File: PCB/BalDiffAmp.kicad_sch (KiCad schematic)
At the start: 19 parts, among them U11 OPA1622

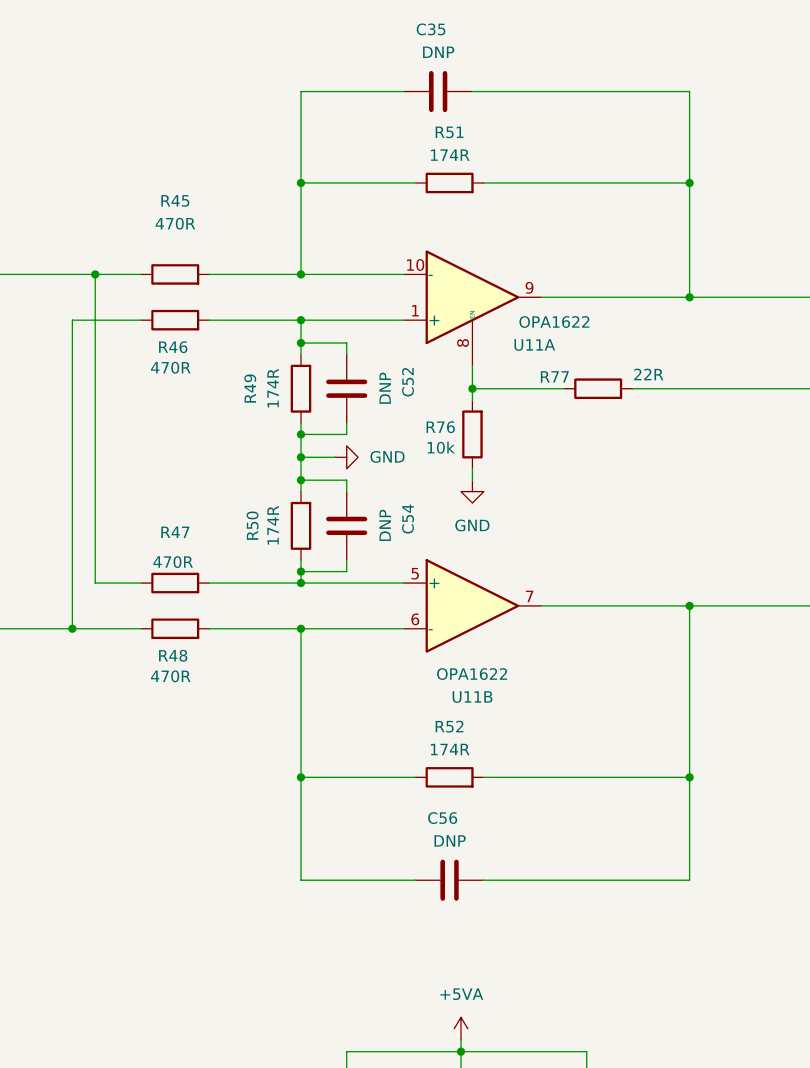
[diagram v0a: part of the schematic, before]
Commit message: Optimized designator positions and DNP for capacitors in OPA1622
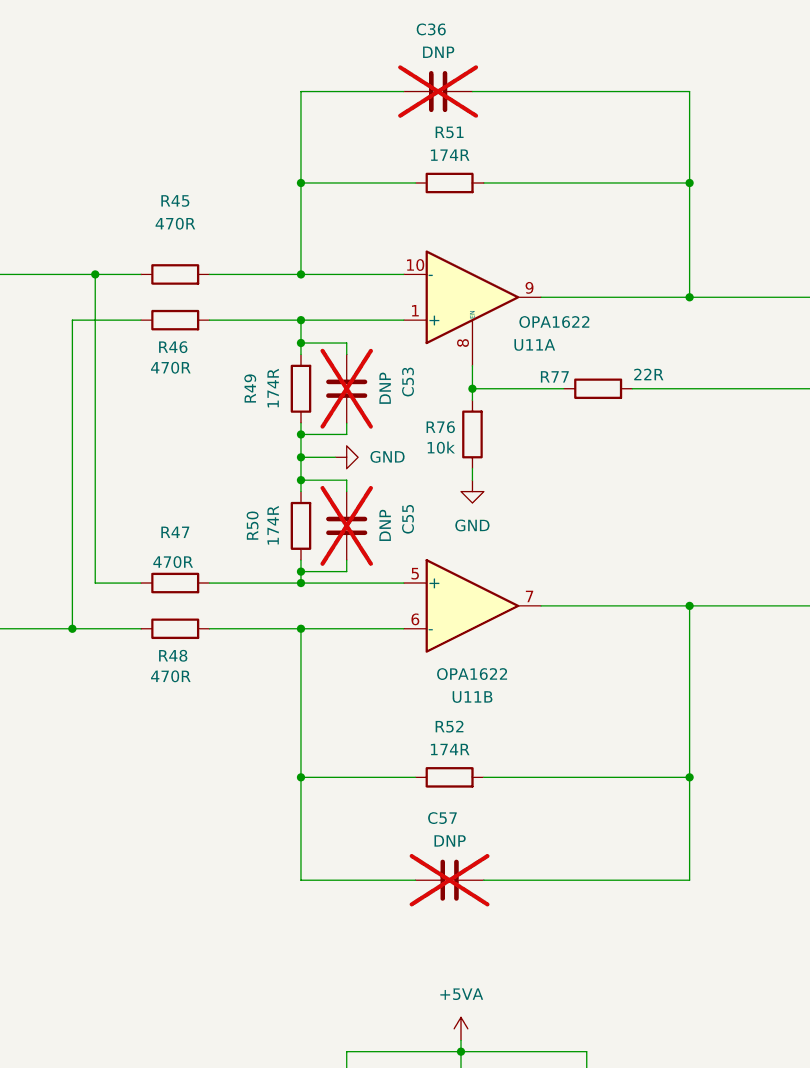
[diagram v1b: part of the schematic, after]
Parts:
- C36: renamed from C35; now not fitted
- C53: renamed from C52; now not fitted
- C55: renamed from C54; now not fitted
- C57: renamed from C56; now not fitted
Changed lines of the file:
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@@
 		(in_bom yes)
 		(on_board yes)
-		(dnp no)
-		(property "Reference" "C35"
+		(dnp yes)
+		(property "Reference" "C36"
 			(at 137.668 28.702 90)
 			(effects
@@
 		(in_bom yes)
 		(on_board yes)
-		(dnp no)
-		(property "Reference" "C54"
+		(dnp yes)
+		(property "Reference" "C55"
 			(at 135.128 83.058 90)
 			(effects
@@
 		(in_bom yes)
 		(on_board yes)
-		(dnp no)
-		(property "Reference" "C52"
+		(dnp yes)
+		(property "Reference" "C53"
 			(at 135.128 67.818 90)
 			(effects
@@
 		(in_bom yes)
 		(on_board yes)
-		(dnp no)
-		(property "Reference" "C56"
+		(dnp yes)
+		(property "Reference" "C57"
 			(at 138.938 116.332 90)
 			(effects

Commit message: Redone placement and layout of OPA1622. Still finishing touches
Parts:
- removed C66, C67: 1uF, Capacitor_SMD:C_0603_1608Metric_Pad1.08x0.95mm_HandSolder, symbol Device:C
- removed R76: 10k, Resistor_SMD:R_0402_1005Metric_Pad0.72x0.64mm_HandSolder, symbol Device:R
- removed R77: 22R, Resistor_SMD:R_0402_1005Metric_Pad0.72x0.64mm_HandSolder, symbol Device:R
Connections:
- net BALDIFFAMP_ENABLE: now also U11.8 (EN)

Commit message: Changed the BOM field for JLCPCB to the original name instead of LCSC
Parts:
- C64, C65: JLCPCB Part # (none) -> C1525; LCSC Part # C1525 -> (none)
- R45, R46, R47, R48: JLCPCB Part # (none) -> C445590; LCSC Part # C445590 -> (none)
- R49, R50, R51, R52: JLCPCB Part # (none) -> C852566; LCSC Part # C852566 -> (none)
- U11: JLCPCB Part # (none) -> C2876559; LCSC Part # C2876559 -> (none)
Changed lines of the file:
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@@
 			)
 		)
-		(property "LCSC Part #" "C852566"
+		(property "JLCPCB Part #" "C852566"
 			(at 139.7 45.72 0)
 			(effects
@@
 			)
 		)
-		(property "LCSC Part #" "C1525"
+		(property "JLCPCB Part #" "C1525"
 			(at 128.27 148.59 0)
 			(effects
@@
 		)
 		(property "Voltage" "50V"
-			(at 138.43 35.56 0)
-			(effects
-				(font
-					(size 1.27 1.27)
-				)
-				(hide yes)
-			)
-		)
-		(property "LCSC Part #" ""
 			(at 138.43 35.56 0)
 			(effects
@@
 			)
 		)
-		(property "LCSC Part #" "C2876559"
+		(property "JLCPCB Part #" "C2876559"
 			(at 142.24 92.71 0)
 			(effects
@@
 			)
 		)
-		(property "LCSC Part #" "C445590"
+		(property "JLCPCB Part #" "C445590"
 			(at 109.22 60.96 0)
 			(effects
@@
 			)
 		)
-		(property "LCSC Part #" ""
-			(at 128.27 83.82 0)
-			(effects
-				(font
-					(size 1.27 1.27)
-				)
-				(hide yes)
-			)
-		)
 		(pin "2"
 		)
@@
 			)
 		)
-		(property "LCSC Part #" "C445590"
+		(property "JLCPCB Part #" "C445590"
 			(at 109.22 95.25 0)
 			(effects
@@
 			)
 		)
-		(property "LCSC Part #" "C2876559"
+		(property "JLCPCB Part #" "C2876559"
 			(at 157.48 152.4 0)
 			(effects
@@
 			)
 		)
-		(property "LCSC Part #" "C1525"
+		(property "JLCPCB Part #" "C1525"
 			(at 128.27 161.29 0)
 			(effects
@@
 			)
 		)
-		(property "LCSC Part #" "C852566"
+		(property "JLCPCB Part #" "C852566"
 			(at 123.19 83.82 0)
 			(effects
@@
 			)
 		)
-		(property "LCSC Part #" "C2876559"
+		(property "JLCPCB Part #" "C2876559"
 			(at 142.24 58.42 0)
 			(effects
@@
 		)
 		(property "Voltage" "50V"
-			(at 128.27 68.58 0)
-			(effects
-				(font
-					(size 1.27 1.27)
-				)
-				(hide yes)
-			)
-		)
-		(property "LCSC Part #" ""
 			(at 128.27 68.58 0)
 			(effects
@@
 			)
 		)
-		(property "LCSC Part #" ""
-			(at 139.7 123.19 0)
-			(effects
-				(font
-					(size 1.27 1.27)
-				)
-				(hide yes)
-			)
-		)
 		(pin "2"
 		)
@@
 			)
 		)
-		(property "LCSC Part #" "C445590"
+		(property "JLCPCB Part #" "C445590"
 			(at 109.22 90.17 0)
 			(effects
@@
 			)
 		)
-		(property "LCSC Part #" "C445590"
+		(property "JLCPCB Part #" "C445590"
 			(at 109.22 55.88 0)
 			(effects
@@
 			)
 		)
-		(property "LCSC Part #" "C852566"
+		(property "JLCPCB Part #" "C852566"
 			(at 139.7 111.76 0)
 			(effects
@@
 			)
 		)
-		(property "LCSC Part #" "C852566"
+		(property "JLCPCB Part #" "C852566"
 			(at 123.19 68.58 0)
 			(effects

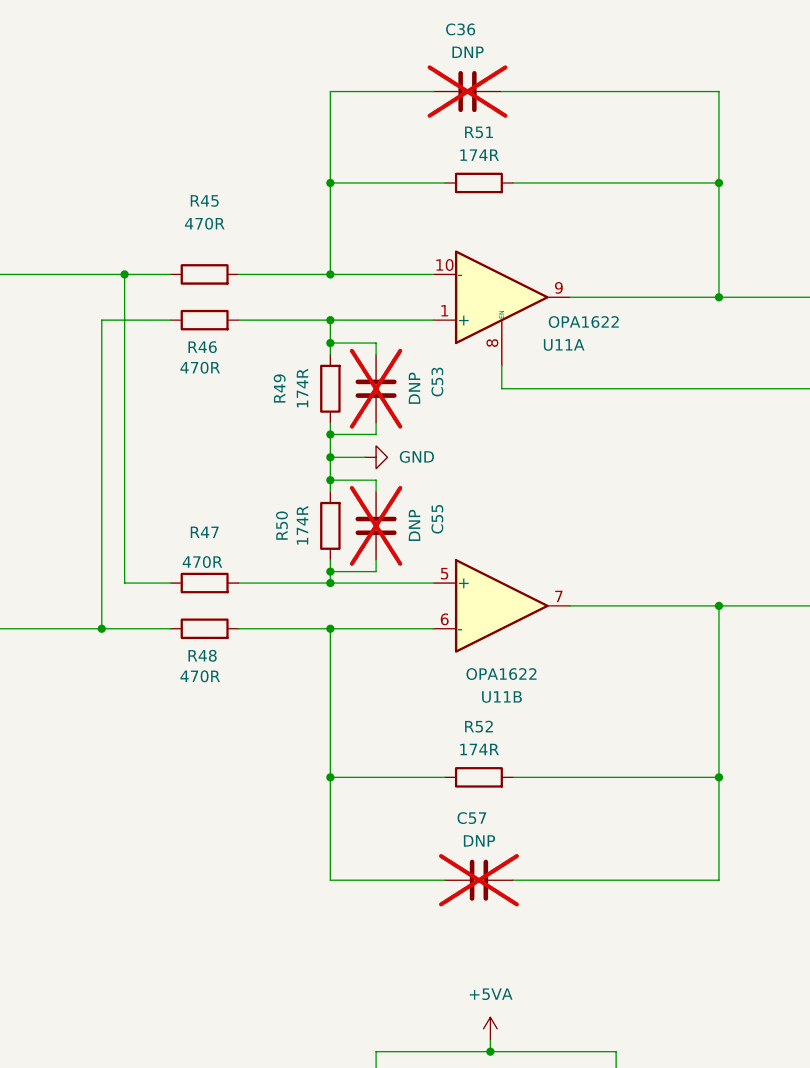
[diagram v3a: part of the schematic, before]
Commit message: Changed single ended connector for gold plated part and changed resistor and capacitor values of opa1622 amp for improved power on high impedance headphones
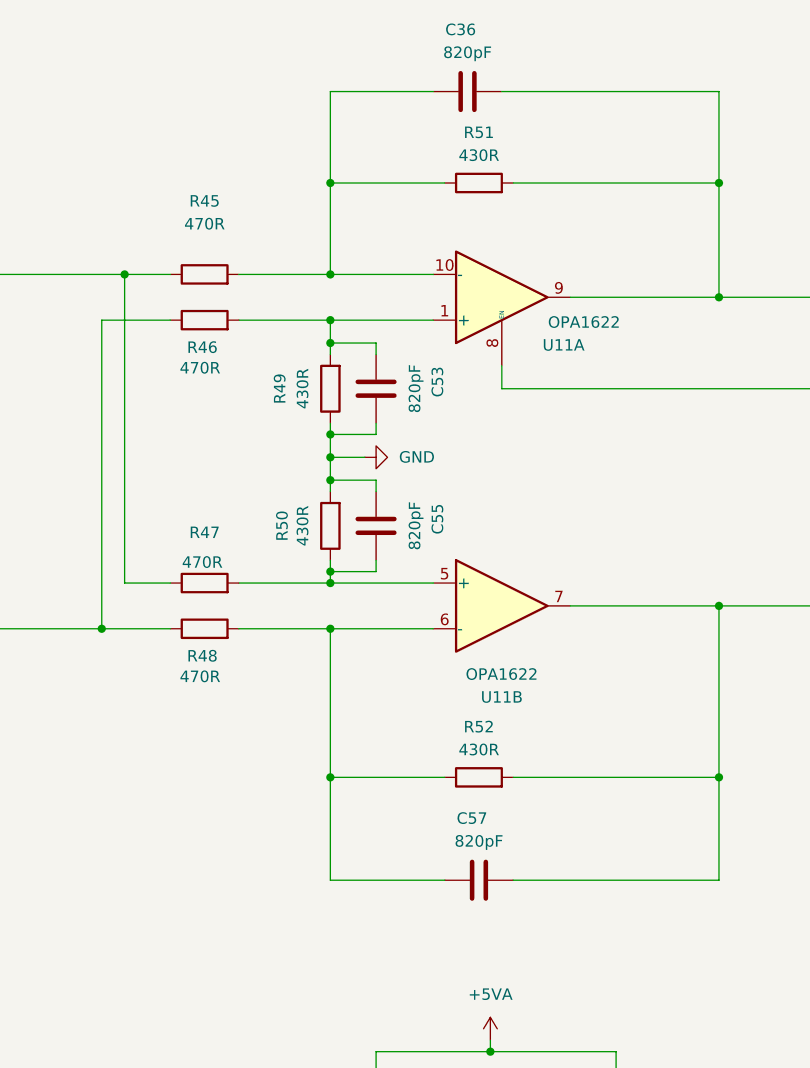
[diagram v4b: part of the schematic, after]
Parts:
- C36, C53, C55, C57: value DNP -> 820pF; JLCPCB Part # (none) -> C99081; now fitted
- R49, R50, R51, R52: value 174R -> 430R; JLCPCB Part # C852566 -> C186317
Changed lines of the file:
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@@
 			)
 		)
-		(property "Value" "174R"
+		(property "Value" "430R"
 			(at 139.7 42.672 90)
 			(effects
@@
 			)
 		)
-		(property "JLCPCB Part #" "C852566"
+		(property "JLCPCB Part #" "C186317"
 			(at 139.7 45.72 0)
 			(effects
@@
 		(in_bom yes)
 		(on_board yes)
-		(dnp yes)
+		(dnp no)
 		(property "Reference" "C36"
 			(at 137.668 28.702 90)
@@
 			)
 		)
-		(property "Value" "DNP"
+		(property "Value" "820pF"
 			(at 138.43 31.242 90)
 			(effects
@@
 		)
 		(property "Voltage" "50V"
+			(at 138.43 35.56 0)
+			(effects
+				(font
+					(size 1.27 1.27)
+				)
+				(hide yes)
+			)
+		)
+		(property "JLCPCB Part #" "C99081"
 			(at 138.43 35.56 0)
 			(effects
@@
 		(in_bom yes)
 		(on_board yes)
-		(dnp yes)
+		(dnp no)
 		(property "Reference" "C55"
 			(at 135.128 83.058 90)
@@
 			)
 		)
-		(property "Value" "DNP"
+		(property "Value" "820pF"
 			(at 132.588 83.82 90)
 			(effects
@@
 		)
 		(property "Voltage" "50V"
+			(at 128.27 83.82 0)
+			(effects
+				(font
+					(size 1.27 1.27)
+				)
+				(hide yes)
+			)
+		)
+		(property "JLCPCB Part #" "C99081"
 			(at 128.27 83.82 0)
 			(effects
@@
 			)
 		)
-		(property "Value" "174R"
+		(property "Value" "430R"
 			(at 120.142 83.82 90)
 			(effects
@@
 			)
 		)
-		(property "JLCPCB Part #" "C852566"
+		(property "JLCPCB Part #" "C186317"
 			(at 123.19 83.82 0)
 			(effects
@@
 		(in_bom yes)
 		(on_board yes)
-		(dnp yes)
+		(dnp no)
 		(property "Reference" "C53"
 			(at 135.128 67.818 90)
@@
 			)
 		)
-		(property "Value" "DNP"
+		(property "Value" "820pF"
 			(at 132.588 68.58 90)
 			(effects
@@
 		)
 		(property "Voltage" "50V"
+			(at 128.27 68.58 0)
+			(effects
+				(font
+					(size 1.27 1.27)
+				)
+				(hide yes)
+			)
+		)
+		(property "JLCPCB Part #" "C99081"
 			(at 128.27 68.58 0)
 			(effects
@@
 		(in_bom yes)
 		(on_board yes)
-		(dnp yes)
+		(dnp no)
 		(property "Reference" "C57"
 			(at 138.938 116.332 90)
@@
 			)
 		)
-		(property "Value" "DNP"
+		(property "Value" "820pF"
 			(at 139.7 118.872 90)
 			(effects
@@
 		)
 		(property "Voltage" "50V"
+			(at 139.7 123.19 0)
+			(effects
+				(font
+					(size 1.27 1.27)
+				)
+				(hide yes)
+			)
+		)
+		(property "JLCPCB Part #" "C99081"
 			(at 139.7 123.19 0)
 			(effects
@@
 			)
 		)
-		(property "Value" "174R"
+		(property "Value" "430R"
 			(at 139.7 108.712 90)
 			(effects
@@
 			)
 		)
-		(property "JLCPCB Part #" "C852566"
+		(property "JLCPCB Part #" "C186317"
 			(at 139.7 111.76 0)
 			(effects
@@
 			)
 		)
-		(property "Value" "174R"
+		(property "Value" "430R"
 			(at 120.142 68.58 90)
 			(effects
@@
 			)
 		)
-		(property "JLCPCB Part #" "C852566"
+		(property "JLCPCB Part #" "C186317"
 			(at 123.19 68.58 0)
 			(effects
